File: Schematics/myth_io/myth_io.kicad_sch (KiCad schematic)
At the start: 8 parts, among them J1 Conn_02x01, U1 74HC14, U2 74LS02, U3 74HC163, U4 74HC238, X1 CXO_DIP14

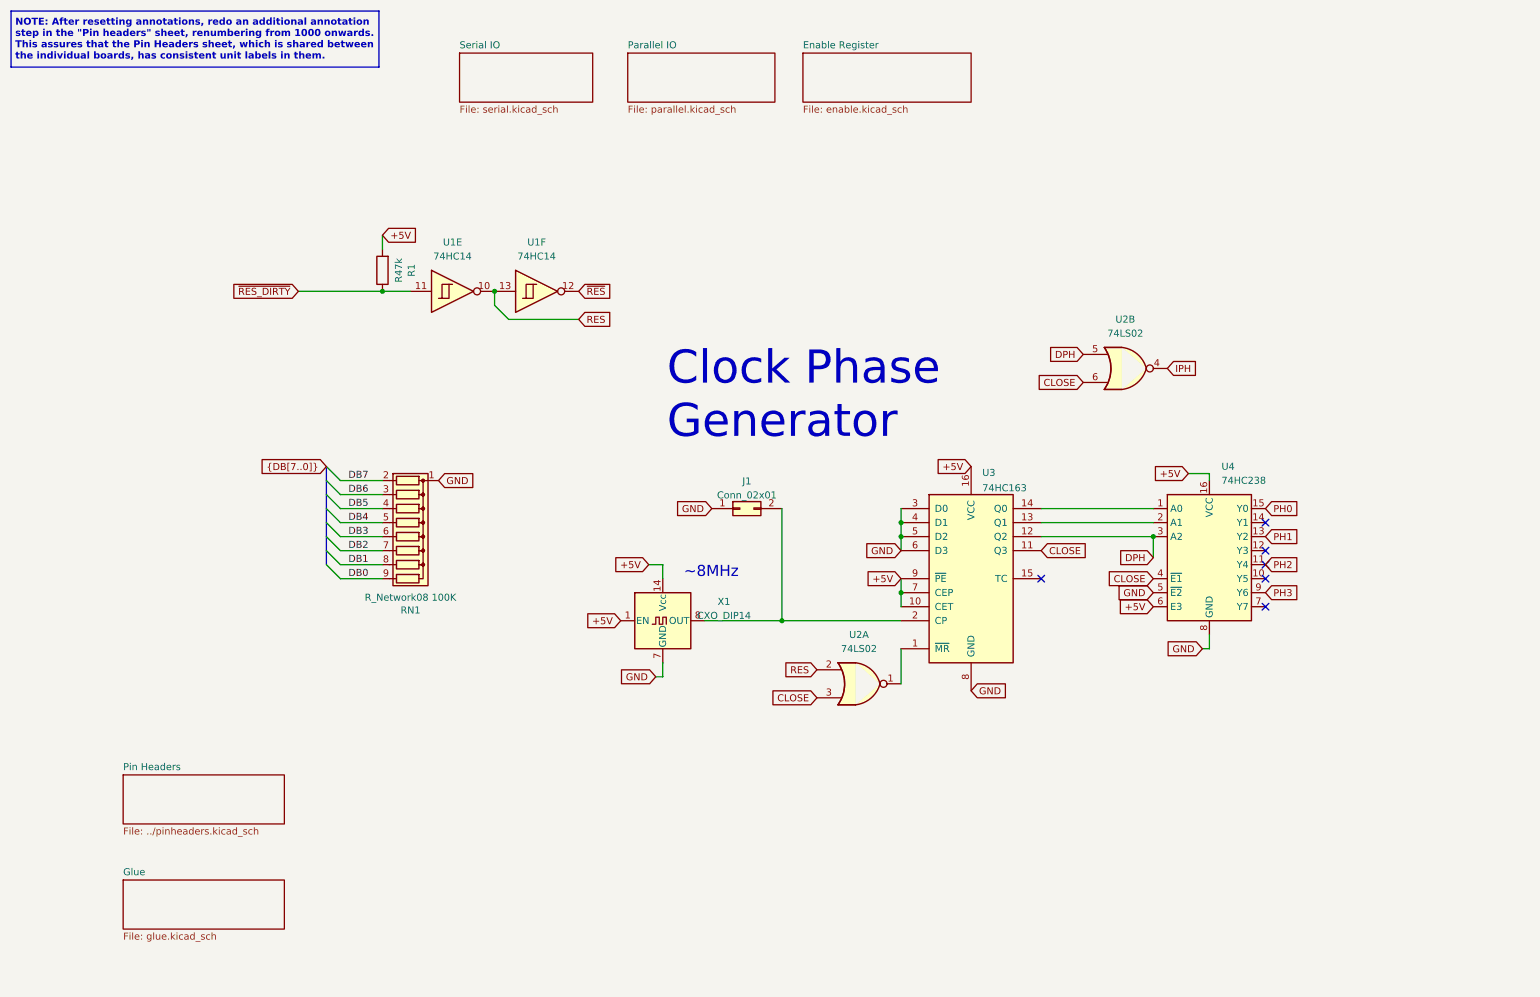
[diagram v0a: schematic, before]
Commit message: Reduce number of shared headers
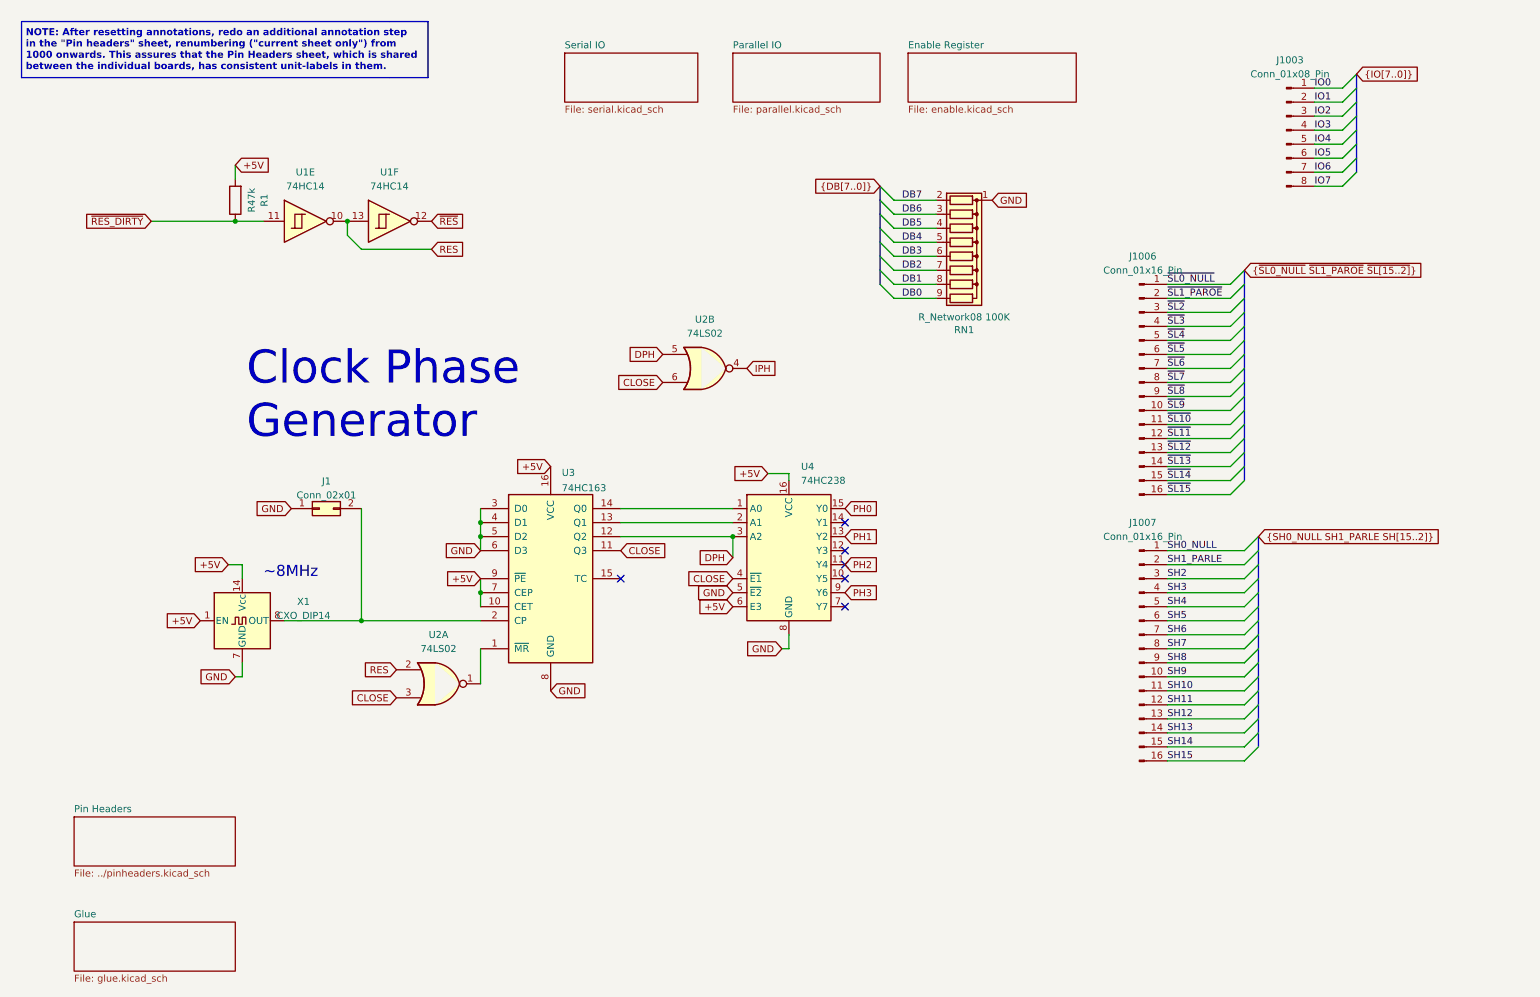
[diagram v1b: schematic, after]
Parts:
- added J1003: Conn_01x08_Pin, symbol Connector:Conn_01x08_Pin
- added J1006, J1007: Conn_01x16_Pin, Connector_PinHeader_2.54mm:PinHeader_1x16_P2.54mm_Vertical, symbol Connector:Conn_01x16_Pin
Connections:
- new net IO0: J1003.1 (Pin_1)
- new net IO1: J1003.2 (Pin_2)
- new net IO2: J1003.3 (Pin_3)
- new net IO3: J1003.4 (Pin_4)
- new net IO4: J1003.5 (Pin_5)
- new net IO5: J1003.6 (Pin_6)
- new net IO6: J1003.7 (Pin_7)
- new net IO7: J1003.8 (Pin_8)
- new net SH0_NULL: J1007.1 (Pin_1)
- new net SH10: J1007.11 (Pin_11)
- new net SH11: J1007.12 (Pin_12)
- new net SH12: J1007.13 (Pin_13)
- new net SH13: J1007.14 (Pin_14)
- new net SH14: J1007.15 (Pin_15)
- new net SH15: J1007.16 (Pin_16)
- new net SH1_PARLE: J1007.2 (Pin_2)
- new net SH2: J1007.3 (Pin_3)
- new net SH3: J1007.4 (Pin_4)
- new net SH4: J1007.5 (Pin_5)
- new net SH5: J1007.6 (Pin_6)
- new net SH6: J1007.7 (Pin_7)
- new net SH7: J1007.8 (Pin_8)
- new net SH8: J1007.9 (Pin_9)
- new net SH9: J1007.10 (Pin_10)
- new net ~{SL0_NULL}: J1006.1 (Pin_1)
- new net ~{SL10}: J1006.11 (Pin_11)
- new net ~{SL11}: J1006.12 (Pin_12)
- new net ~{SL12}: J1006.13 (Pin_13)
- new net ~{SL13}: J1006.14 (Pin_14)
- new net ~{SL14}: J1006.15 (Pin_15)
- new net ~{SL15}: J1006.16 (Pin_16)
- new net ~{SL1_PAROE}: J1006.2 (Pin_2)
- new net ~{SL2}: J1006.3 (Pin_3)
- new net ~{SL3}: J1006.4 (Pin_4)
- new net ~{SL4}: J1006.5 (Pin_5)
- new net ~{SL5}: J1006.6 (Pin_6)
- new net ~{SL6}: J1006.7 (Pin_7)
- new net ~{SL7}: J1006.8 (Pin_8)
- new net ~{SL8}: J1006.9 (Pin_9)
- new net ~{SL9}: J1006.10 (Pin_10)
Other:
- note added: "NOTE: After resetting annotations, redo an additional annotation step in the "Pin headers" sheet, renumbering ("current sheet only") from 1000 onwards. This assures that the Pin Headers sheet, which is shared between the individual boards, has consistent unit-labels in them."
- note removed: "NOTE: After resetting annotations, redo an additional annotation step in the "Pin headers" sheet, renumbering from 1000 onwards. This assures that the Pin Headers sheet, which is shared between the individual boards, has consistent unit labels in them."
- moved on the sheet: J1, R1, RN1, U1E, U1F, U2A, U2B, U3, U4, X1

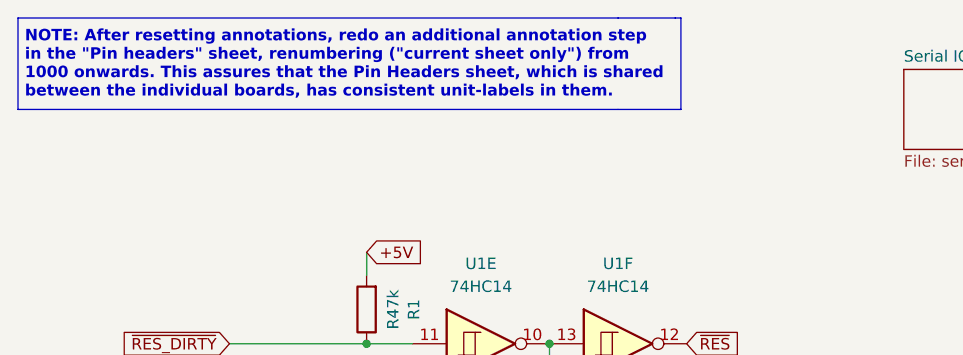
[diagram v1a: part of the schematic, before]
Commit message: Improve schematics for readability
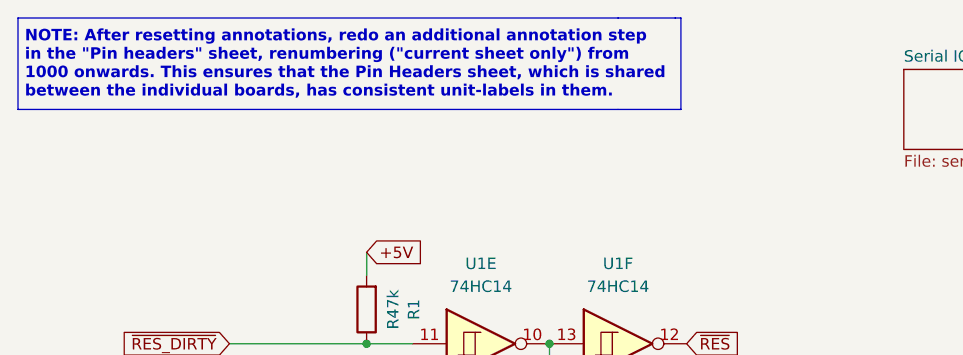
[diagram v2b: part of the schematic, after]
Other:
- note added: "NOTE: After resetting annotations, redo an additional annotation step in the "Pin headers" sheet, renumbering ("current sheet only") from 1000 onwards. This ensures that the Pin Headers sheet, which is shared between the individual boards, has consistent unit-labels in them."
- note removed: "NOTE: After resetting annotations, redo an additional annotation step in the "Pin headers" sheet, renumbering ("current sheet only") from 1000 onwards. This assures that the Pin Headers sheet, which is shared between the individual boards, has consistent unit-labels in them."
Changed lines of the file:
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@@
 		)
 	)
-	(text "NOTE: After resetting annotations, redo an additional annotation step\nin the \"Pin headers\" sheet, renumbering (\"current sheet only\") from\n1000 onwards. This assures that the Pin Headers sheet, which is shared\nbetween the individual boards, has consistent unit-labels in them."
+	(text "NOTE: After resetting annotations, redo an additional annotation step\nin the \"Pin headers\" sheet, renumbering (\"current sheet only\") from\n1000 onwards. This ensures that the Pin Headers sheet, which is shared\nbetween the individual boards, has consistent unit-labels in them."
 		(exclude_from_sim no)
 		(at 16.637 24.892 0)

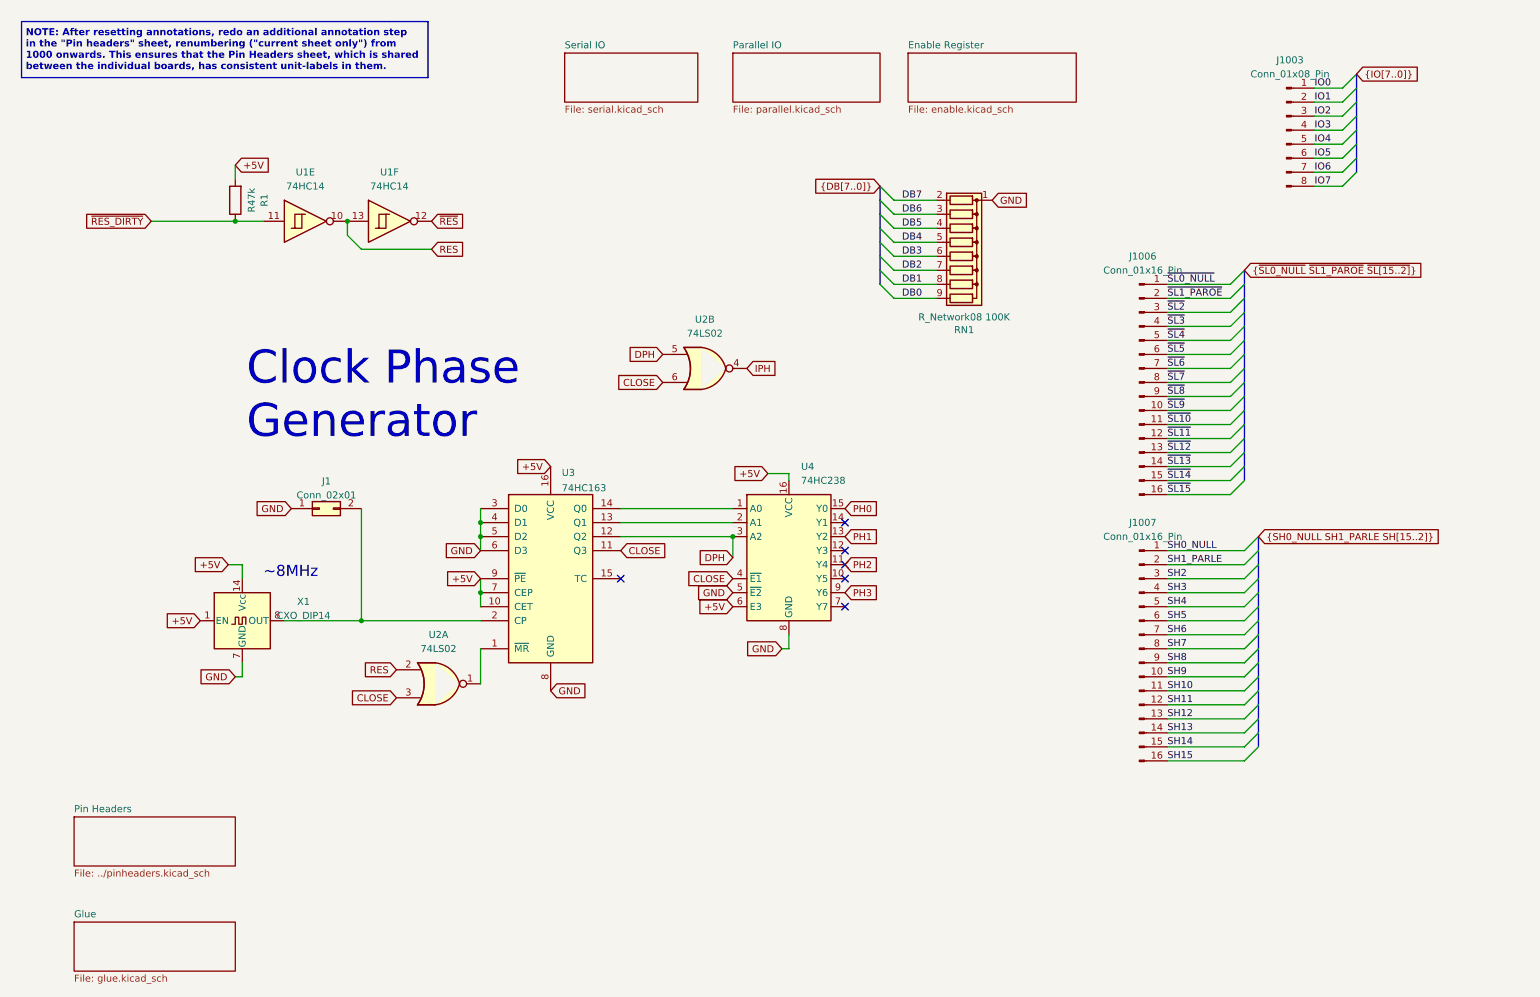
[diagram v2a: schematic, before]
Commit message: Change d to g
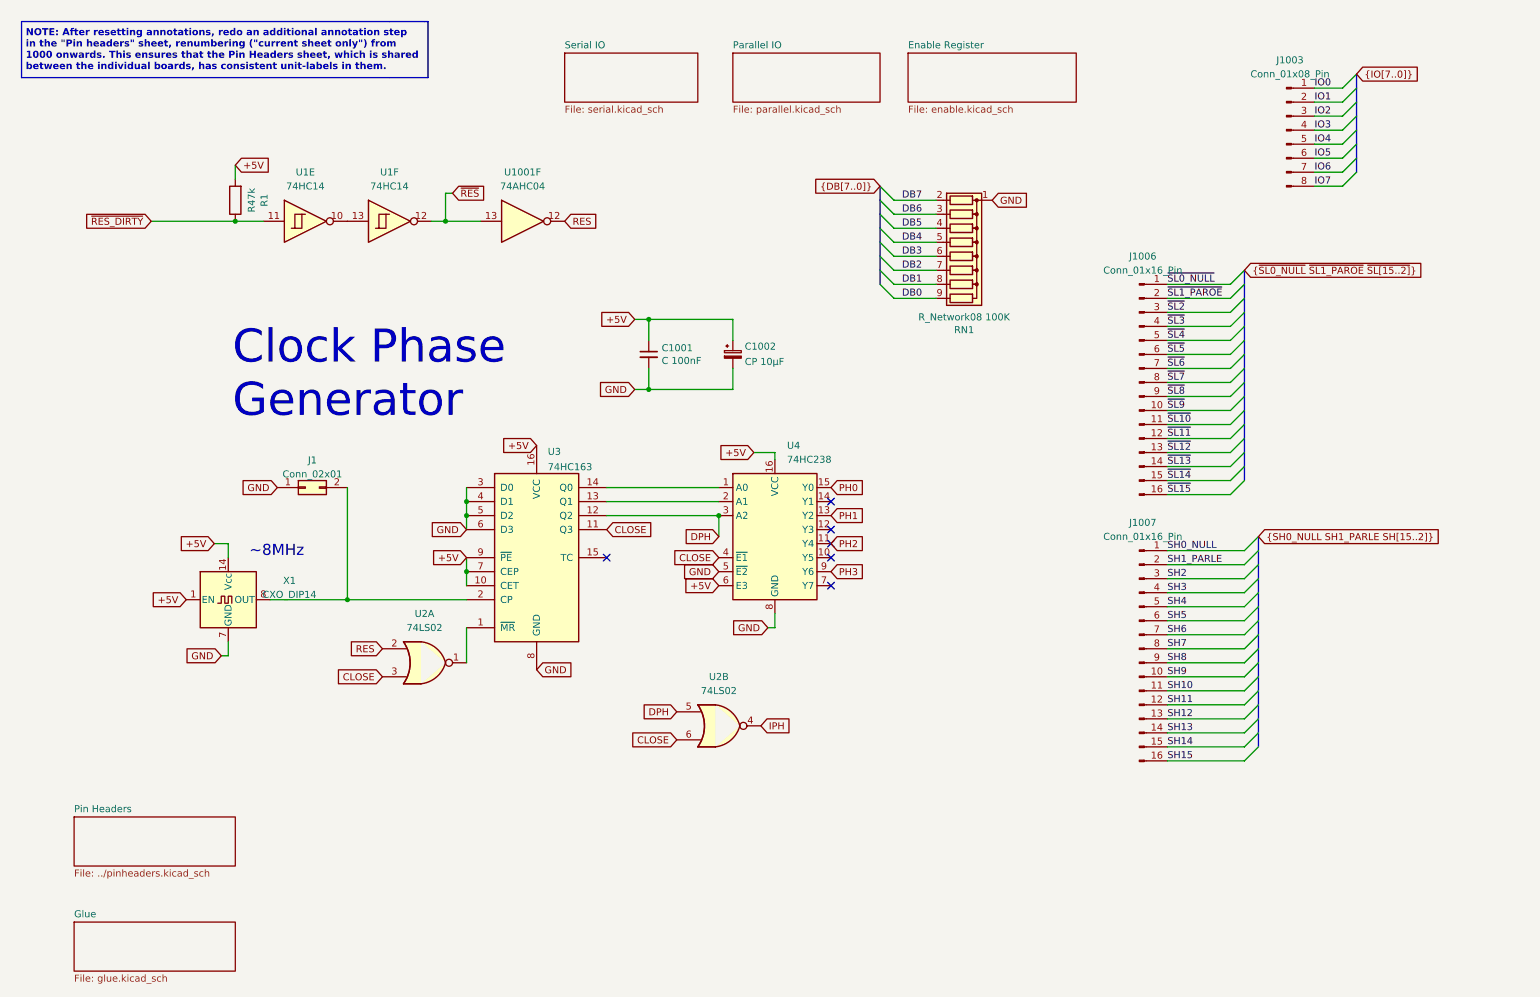
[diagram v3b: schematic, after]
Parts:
- added C1001: C 100nF, Capacitor_THT:C_Disc_D5.0mm_W2.5mm_P2.50mm, symbol Device:C_Small
- added C1002: CP 10μF, Capacitor_THT:CP_Radial_D6.3mm_P2.50mm, symbol Device:C_Polarized_Small
- added U1001: 74AHC04, Package_DIP:DIP-14_W7.62mm_Socket_LongPads, symbol 74xx:74AHC04
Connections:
- net +5V: now also C1001.1, C1002.1
- net GND: now also C1001.2, C1002.2
- net RES: now also U1001.12; no longer U1.10, U1.13
- net ~{RES}: now also U1001.13
- new net: U1.10, U1.13
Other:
- moved on the sheet: J1, U2A, U2B, U3, U4, X1
